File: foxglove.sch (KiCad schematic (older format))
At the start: 96 parts, among them IC1 LFE5U-12F-6BG256C, J1 NEIGHBOR1, J2 NEIGHBOR2, J3 Conn_02x05_Odd_Even, J4 Conn_02x10_Odd_Even, J5 Conn_01x02_Female, J6 Conn_02x03_Odd_Even, J7 BONUS_ROW, U1 LM393, U2 ADP225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

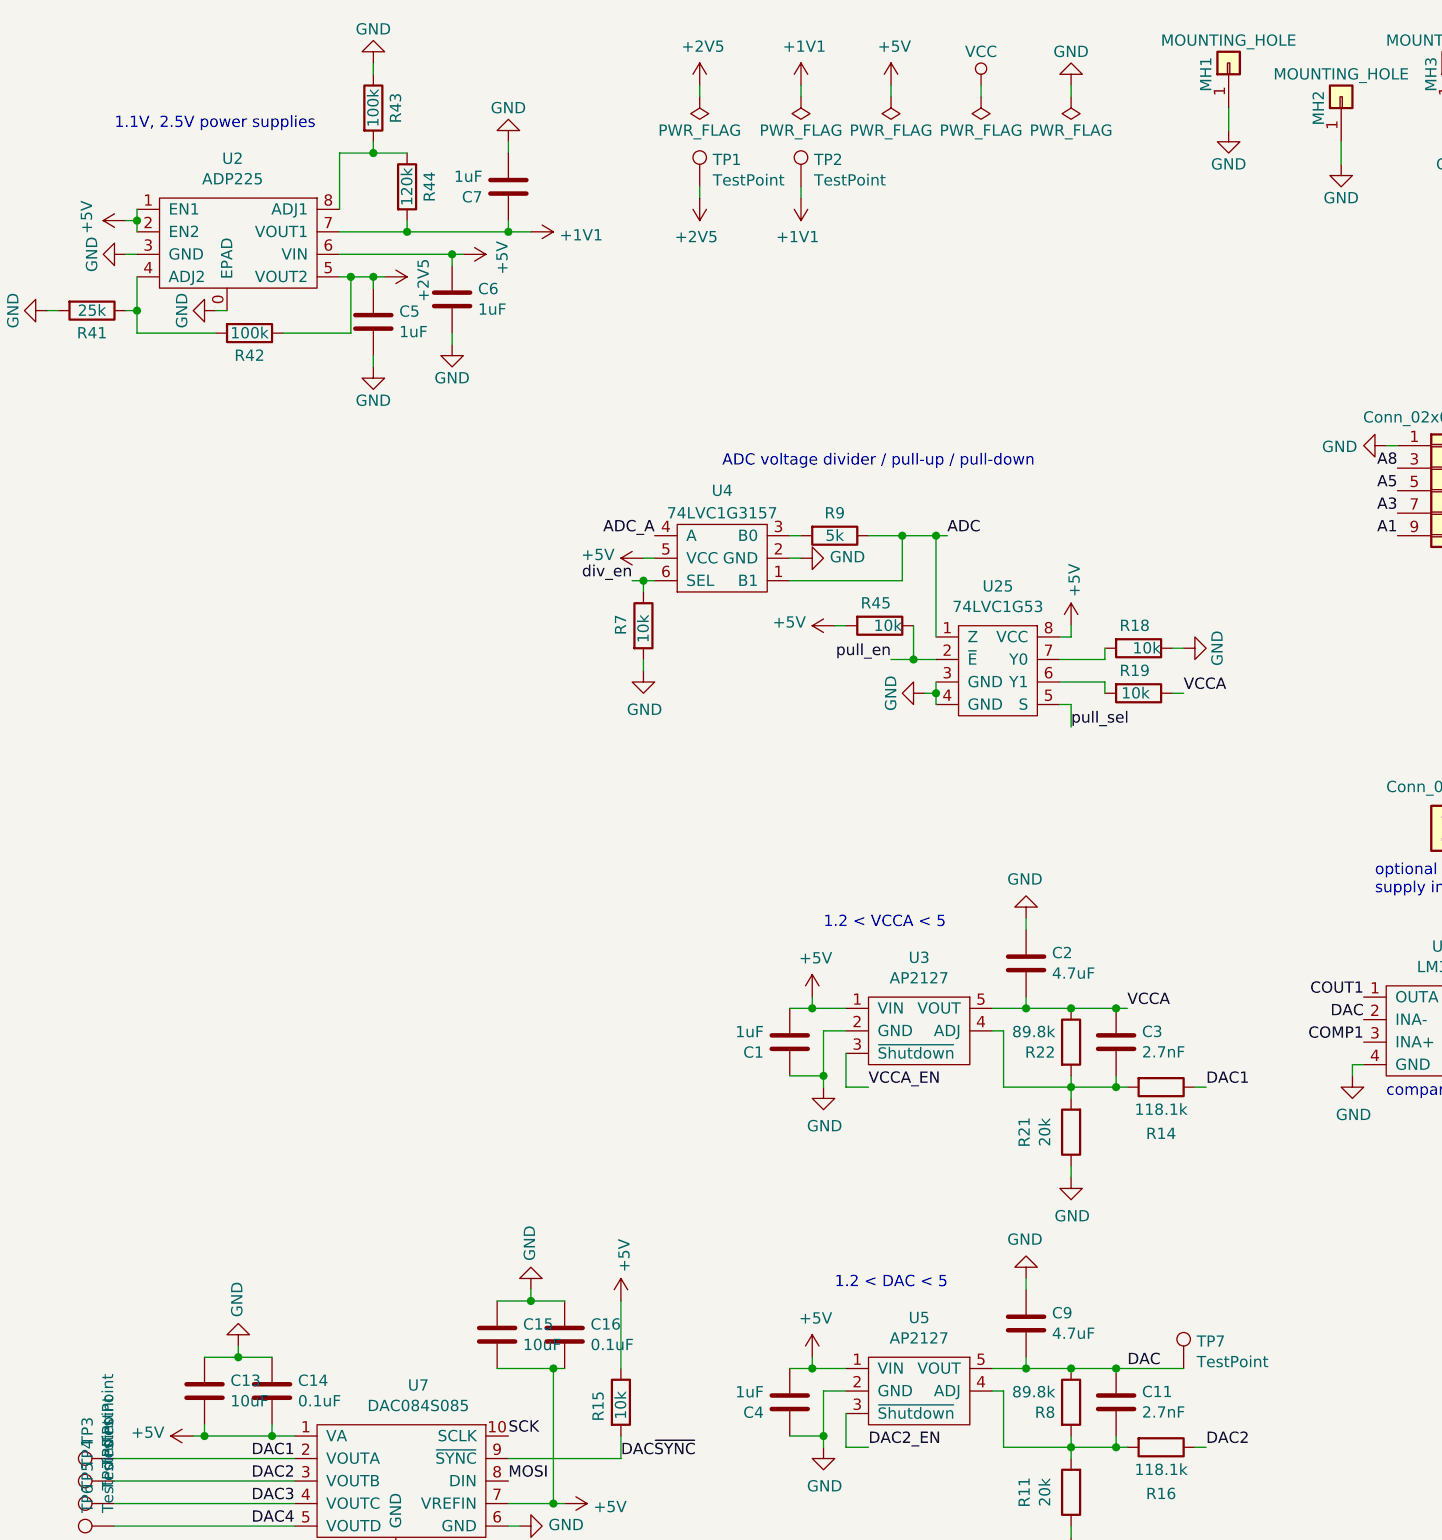
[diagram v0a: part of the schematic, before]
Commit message: Improved silkscreen table visibility and changed board edge cuts to support right-angle connectors
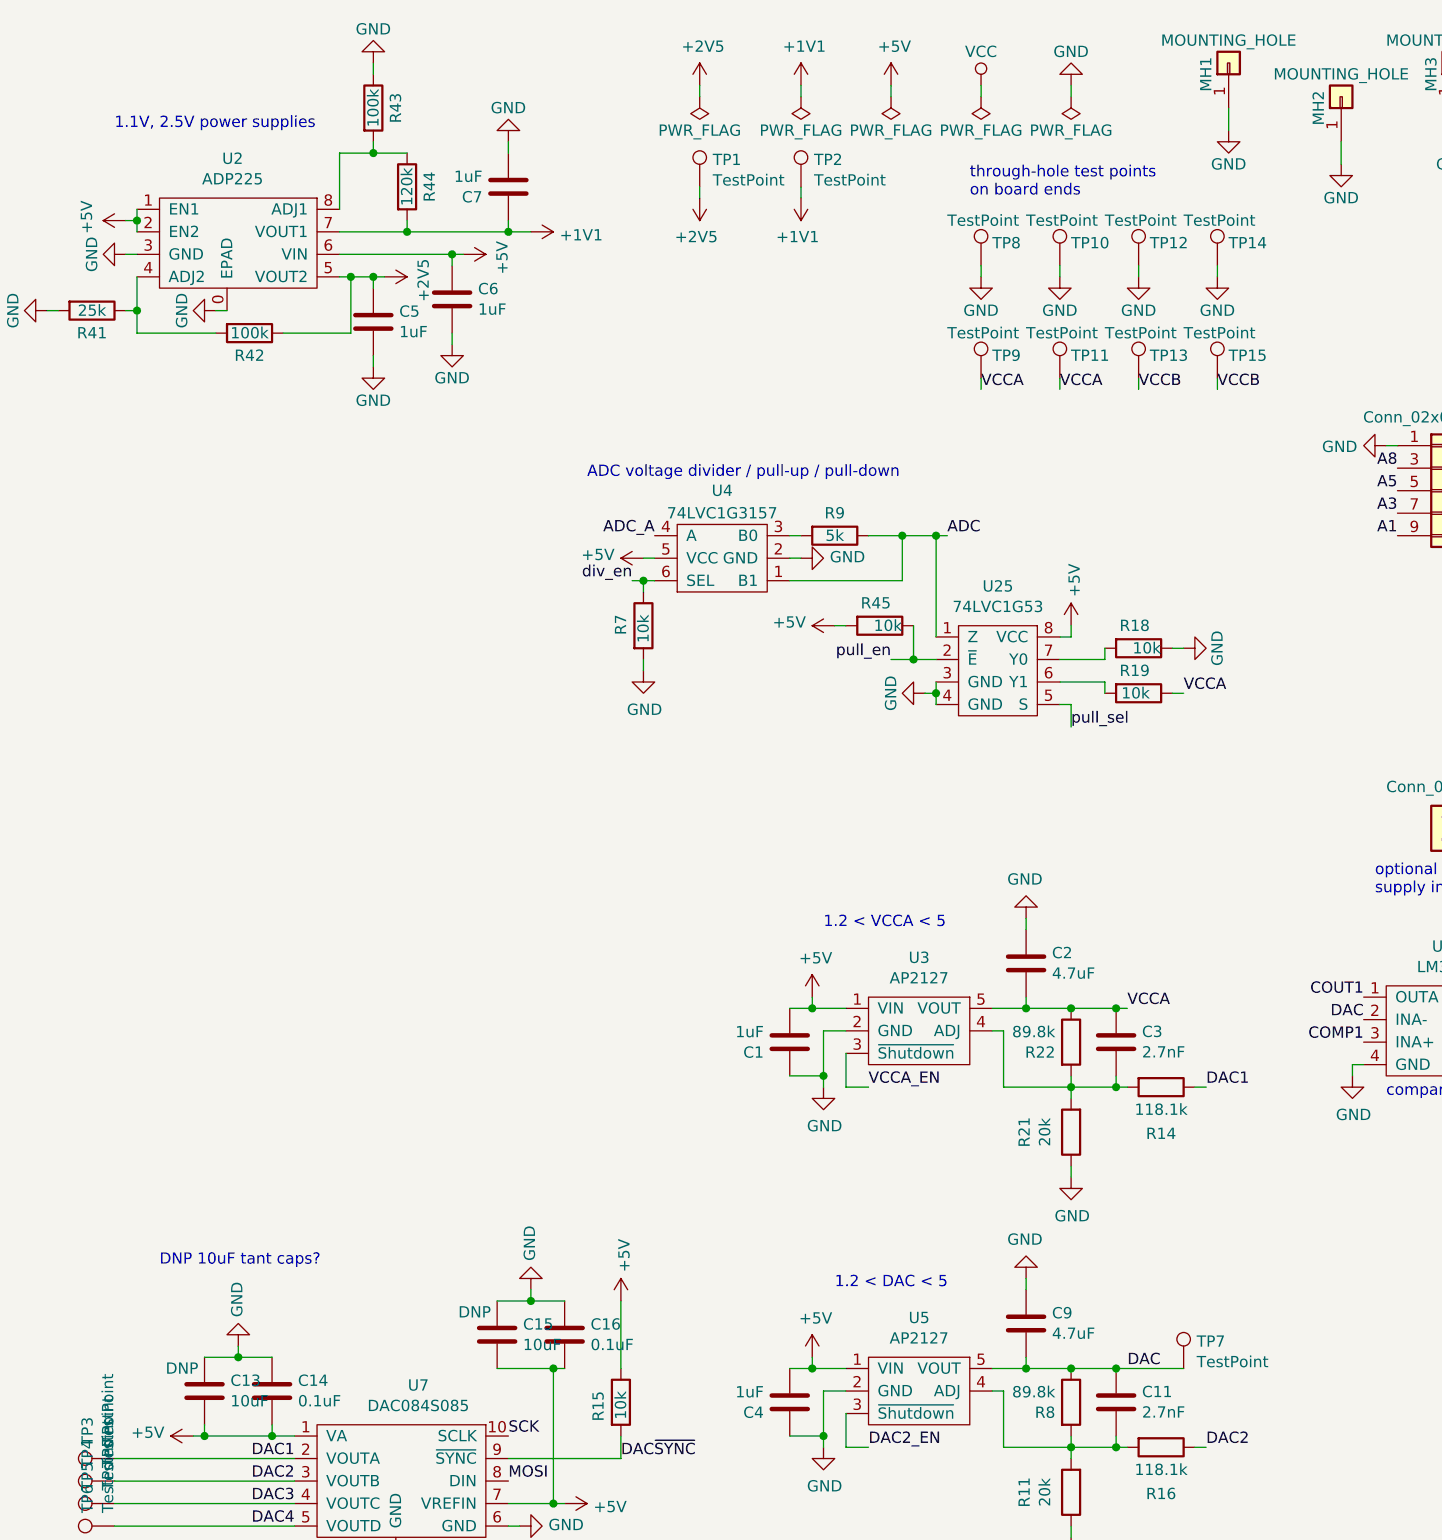
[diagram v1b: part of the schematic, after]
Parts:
- added TP10, TP12, TP14, TP8: TestPoint, gsg-modules:HEADER-1x1, symbol Connector:TestPoint
- added TP11, TP13, TP15, TP9: TestPoint, gsg-modules:HEADER-1x1-TESTPROBE, symbol Connector:TestPoint
- C13, C15: Note (none) -> DNP
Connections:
- net GND: now also TP10.1, TP12.1, TP14.1, TP8.1
- net VCCA: now also TP11.1, TP9.1
- net VCCB: now also TP13.1, TP15.1
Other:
- note added: "DNP 10uF tant caps?"
- note added: "through-hole test points\non board ends"
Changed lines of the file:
@@
 F 5 "F981A106MMA" H 10050 6700 50  0001 C CNN "Part Number"
 F 6 "CAP TANT 10UF 20% 10V 0603  " H 10050 6700 50  0001 C CNN "Description"
+F 7 "DNP" H 10150 6600 50  0000 C CNN "Note"
 	1    10050 6700
 	-1   0    0    1
@@
 Text Notes 12700 7800 0    50   ~ 0
 1.14 <VCCB < 3.465
-Text Notes 12350 2600 0    50   ~ 0
+Text Notes 11750 2650 0    50   ~ 0
 ADC voltage divider / pull-up / pull-down
 Text Notes 9650 1100 0    50   ~ 0
@@
 F 5 "F981A106MMA" H 11350 6450 50  0001 C CNN "Part Number"
 F 6 "CAP TANT 10UF 20% 10V 0603  " H 11350 6450 50  0001 C CNN "Description"
+F 7 "DNP" H 11450 6350 50  0000 C CNN "Note"
 	1    11350 6450
 	-1   0    0    1
@@
 	0    1    1    0
 $EndComp
-Wire Bus Line
-	-5400 2700 -3400 2700
-Wire Bus Line
-	-5700 3800 -3400 3800
-Wire Bus Line
-	-13800 8000 -10900 8000
-Wire Bus Line
-	-12700 9100 -10900 9100
-Wire Bus Line
-	-2150 4150 -400 4150
 $Comp
 L Device:R R?
@@
 	0    1    1    0
 $EndComp
+$Comp
+L Connector:TestPoint TP8
+U 1 1 5D434205
+P 13500 1700
+F 0 "TP8" H 13550 1800 50  0000 L CNN
+F 1 "TestPoint" H 13350 1900 50  0000 L CNN
+F 2 "gsg-modules:HEADER-1x1" H 13700 1700 50  0001 C CNN
+F 3 "~" H 13700 1700 50  0001 C CNN
+	1    13500 1700
+	1    0    0    -1
+$EndComp
+$Comp
+L power:GND #PWR0140
+U 1 1 5D4347AB
+P 13500 1750
+F 0 "#PWR0140" H 13500 1500 50  0001 C CNN
+F 1 "GND" H 13500 1600 50  0000 C CNN
+F 2 "" H 13500 1750 50  0001 C CNN
+F 3 "" H 13500 1750 50  0001 C CNN
+	1    13500 1750
+	1    0    0    -1
+$EndComp
+Wire Wire Line
+	13500 1700 13500 1750
+$Comp
+L Connector:TestPoint TP10
+U 1 1 5D4A93E9
+P 13850 1700
+F 0 "TP10" H 13900 1800 50  0000 L CNN
+F 1 "TestPoint" H 13700 1900 50  0000 L CNN
+F 2 "gsg-modules:HEADER-1x1" H 14050 1700 50  0001 C CNN
+F 3 "~" H 14050 1700 50  0001 C CNN
+	1    13850 1700
+	1    0    0    -1
+$EndComp
+$Comp
+L power:GND #PWR0141
+U 1 1 5D4A93F0
+P 13850 1750
+F 0 "#PWR0141" H 13850 1500 50  0001 C CNN
+F 1 "GND" H 13850 1600 50  0000 C CNN
+F 2 "" H 13850 1750 50  0001 C CNN
+F 3 "" H 13850 1750 50  0001 C CNN
+	1    13850 1750
+	1    0    0    -1
+$EndComp
+Wire Wire Line
+	13850 1700 13850 1750
+$Comp
+L Connector:TestPoint TP12
+U 1 1 5D4E3991
+P 14200 1700
+F 0 "TP12" H 14250 1800 50  0000 L CNN
+F 1 "TestPoint" H 14050 1900 50  0000 L CNN
+F 2 "gsg-modules:HEADER-1x1" H 14400 1700 50  0001 C CNN
+F 3 "~" H 14400 1700 50  0001 C CNN
+	1    14200 1700
+	1    0    0    -1
+$EndComp
+$Comp
+L power:GND #PWR0142
+U 1 1 5D4E3998
+P 14200 1750
+F 0 "#PWR0142" H 14200 1500 50  0001 C CNN
+F 1 "GND" H 14200 1600 50  0000 C CNN
+F 2 "" H 14200 1750 50  0001 C CNN
+F 3 "" H 14200 1750 50  0001 C CNN
+	1    14200 1750
+	1    0    0    -1
+$EndComp
+Wire Wire Line
+	14200 1700 14200 1750
+$Comp
+L Connector:TestPoint TP14
+U 1 1 5D4E399F
+P 14550 1700
+F 0 "TP14" H 14600 1800 50  0000 L CNN
+F 1 "TestPoint" H 14400 1900 50  0000 L CNN
+F 2 "gsg-modules:HEADER-1x1" H 14750 1700 50  0001 C CNN
+F 3 "~" H 14750 1700 50  0001 C CNN
+	1    14550 1700
+	1    0    0    -1
+$EndComp
+$Comp
+L power:GND #PWR0143
+U 1 1 5D4E39A6
+P 14550 1750
+F 0 "#PWR0143" H 14550 1500 50  0001 C CNN
+F 1 "GND" H 14550 1600 50  0000 C CNN
+F 2 "" H 14550 1750 50  0001 C CNN
+F 3 "" H 14550 1750 50  0001 C CNN
+	1    14550 1750
+	1    0    0    -1
+$EndComp
+Wire Wire Line
+	14550 1700 14550 1750
+$Comp
+L Connector:TestPoint TP9
+U 1 1 5D55A260
+P 13500 2200
+F 0 "TP9" H 13550 2300 50  0000 L CNN
+F 1 "TestPoint" H 13350 2400 50  0000 L CNN
+F 2 "gsg-modules:HEADER-1x1-TESTPROBE" H 13700 2200 50  0001 C CNN
+F 3 "~" H 13700 2200 50  0001 C CNN
+	1    13500 2200
+	1    0    0    -1
+$EndComp
+Wire Wire Line
+	13500 2200 13500 2250
+$Comp
+L Connector:TestPoint TP11
+U 1 1 5D55A26E
+P 13850 2200
+F 0 "TP11" H 13900 2300 50  0000 L CNN
+F 1 "TestPoint" H 13700 2400 50  0000 L CNN
+F 2 "gsg-modules:HEADER-1x1-TESTPROBE" H 14050 2200 50  0001 C CNN
+F 3 "~" H 14050 2200 50  0001 C CNN
+	1    13850 2200
+	1    0    0    -1
+$EndComp
+Wire Wire Line
+	13850 2200 13850 2250
+$Comp
+L Connector:TestPoint TP13
+U 1 1 5D55A27C
+P 14200 2200
+F 0 "TP13" H 14250 2300 50  0000 L CNN
+F 1 "TestPoint" H 14050 2400 50  0000 L CNN
+F 2 "gsg-modules:HEADER-1x1-TESTPROBE" H 14400 2200 50  0001 C CNN
+F 3 "~" H 14400 2200 50  0001 C CNN
+	1    14200 2200
+	1    0    0    -1
+$EndComp
+Wire Wire Line
+	14200 2200 14200 2250
+$Comp
+L Connector:TestPoint TP15
+U 1 1 5D55A28A
+P 14550 2200
+F 0 "TP15" H 14600 2300 50  0000 L CNN
+F 1 "TestPoint" H 14400 2400 50  0000 L CNN
+F 2 "gsg-modules:HEADER-1x1-TESTPROBE" H 14750 2200 50  0001 C CNN
+F 3 "~" H 14750 2200 50  0001 C CNN
+	1    14550 2200
+	1    0    0    -1
+$EndComp
+Wire Wire Line
+	14550 2200 14550 2250
+Wire Bus Line
+	-5400 2700 -3400 2700
+Wire Bus Line
+	-5700 3800 -3400 3800
+Wire Bus Line
+	-13800 8000 -10900 8000
+Wire Bus Line
+	-12700 9100 -10900 9100
+Wire Bus Line
+	-2150 4150 -400 4150
+Text Label 13500 2250 0    50   ~ 0
+VCCA
+Text Label 13850 2250 0    50   ~ 0
+VCCA
+Text Label 14200 2250 0    50   ~ 0
+VCCB
+Text Label 14550 2250 0    50   ~ 0
+VCCB
+Text Notes 13450 1400 0    50   ~ 0
+through-hole test points\non board ends
+Text Notes 9850 6150 0    50   ~ 0
+DNP 10uF tant caps?
 $EndSCHEMATC

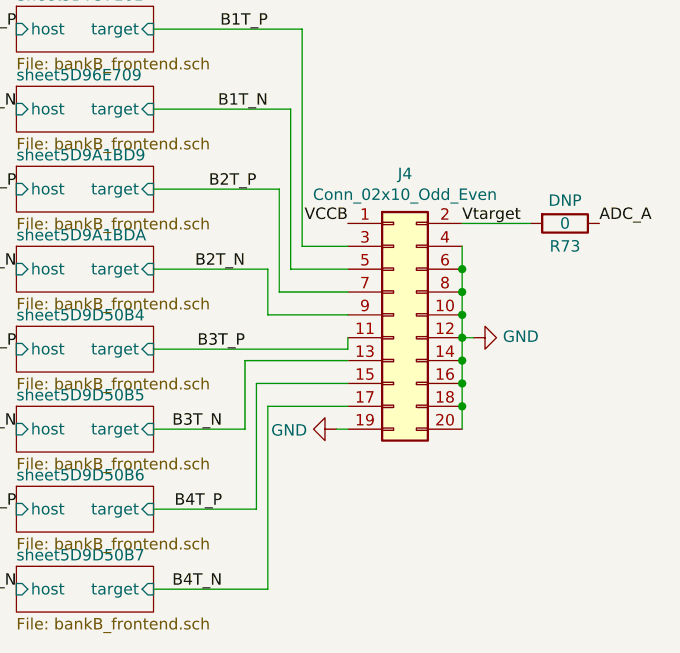
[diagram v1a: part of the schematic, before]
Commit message: Flipped J4 footprint
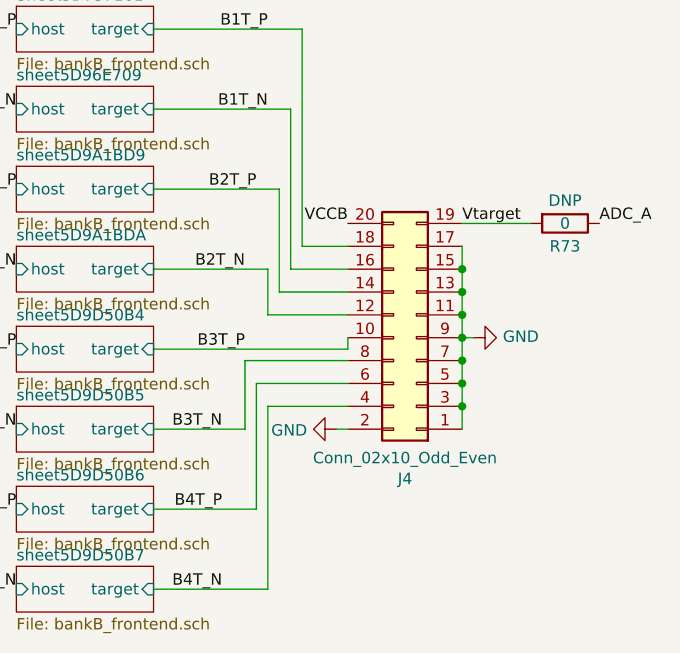
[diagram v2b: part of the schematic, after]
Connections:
- net B1T_N: now also J4.16 (Pin_16); no longer J4.5 (Pin_5)
- net B1T_P: now also J4.18 (Pin_18); no longer J4.3 (Pin_3)
- net B2T_N: now also J4.12 (Pin_12); no longer J4.9 (Pin_9)
- net B2T_P: now also J4.14 (Pin_14); no longer J4.7 (Pin_7)
- net B3T_N: now also J4.8 (Pin_8); no longer J4.13 (Pin_13)
- net B3T_P: now also J4.10 (Pin_10); no longer J4.11 (Pin_11)
- net B4T_N: now also J4.4 (Pin_4); no longer J4.17 (Pin_17)
- net B4T_P: now also J4.6 (Pin_6); no longer J4.15 (Pin_15)
- net GND: now also J4.1 (Pin_1), J4.11 (Pin_11), J4.13 (Pin_13), J4.15 (Pin_15), J4.17 (Pin_17), J4.2 (Pin_2), J4.3 (Pin_3), J4.5 (Pin_5), J4.7 (Pin_7), J4.9 (Pin_9); no longer J4.10 (Pin_10), J4.12 (Pin_12), J4.14 (Pin_14), J4.16 (Pin_16), J4.18 (Pin_18), J4.19 (Pin_19), J4.20 (Pin_20), J4.4 (Pin_4), J4.6 (Pin_6), J4.8 (Pin_8)
- net VCCB: now also J4.20 (Pin_20); no longer J4.1 (Pin_1)
- net Vtarget: now also J4.19 (Pin_19); no longer J4.2 (Pin_2)
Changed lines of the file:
@@
 L Connector_Generic:Conn_02x10_Odd_Even J4
 U 1 1 5D4FD960
-P 19350 1450
-F 0 "J4" H 19400 2067 50  0000 C CNN
-F 1 "Conn_02x10_Odd_Even" H 19400 1976 50  0000 C CNN
-F 2 "Connector_PinHeader_2.54mm:PinHeader_2x10_P2.54mm_Vertical" H 19350 1450 50  0001 C CNN
-F 3 "~" H 19350 1450 50  0001 C CNN
-F 4 "Sullins Connector Solutions" H 19350 1450 50  0001 C CNN "Manufacturer"
-F 5 "SBH11-PBPC-D10-RA-BK" H 19350 1450 50  0001 C CNN "Part Number"
-F 6 "CONN HEADER R/A 20POS 2.54MM" H 19350 1450 50  0001 C CNN "Description"
-	1    19350 1450
-	1    0    0    -1
+P 19450 1550
+F 0 "J4" H 19500 2167 50  0000 C CNN
+F 1 "Conn_02x10_Odd_Even" H 19500 2076 50  0000 C CNN
+F 2 "Connector_PinHeader_2.54mm:PinHeader_2x10_P2.54mm_Vertical" H 19450 1550 50  0001 C CNN
+F 3 "~" H 19450 1550 50  0001 C CNN
+F 4 "Sullins Connector Solutions" H 19450 1550 50  0001 C CNN "Manufacturer"
+F 5 "SBH11-PBPC-D10-RA-BK" H 19450 1550 50  0001 C CNN "Part Number"
+F 6 "CONN HEADER R/A 20POS 2.54MM" H 19450 1550 50  0001 C CNN "Description"
+	1    19450 1550
+	-1   0    0    1
 $EndComp
 Text Label 19150 1050 2    50   ~ 0
@@
 Wire Wire Line
 	14550 2200 14550 2250
-Wire Bus Line
-	-5400 2700 -3400 2700
-Wire Bus Line
-	-5700 3800 -3400 3800
-Wire Bus Line
-	-13800 8000 -10900 8000
-Wire Bus Line
-	-12700 9100 -10900 9100
-Wire Bus Line
-	-2150 4150 -400 4150
 Text Label 13500 2250 0    50   ~ 0
 VCCA
@@
 Text Notes 9850 6150 0    50   ~ 0
 DNP 10uF tant caps?
+Wire Bus Line
+	-5400 2700 -3400 2700
+Wire Bus Line
+	-5700 3800 -3400 3800
+Wire Bus Line
+	-13800 8000 -10900 8000
+Wire Bus Line
+	-12700 9100 -10900 9100
+Wire Bus Line
+	-2150 4150 -400 4150
 $EndSCHEMATC

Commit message: schematic: cleanup and squish onto a page
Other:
- note added: "Analog Frontend"
- note added: "Bank A"
- note added: "Bank B"
- note added: "Digital Frontend"
- note added: "FPGA"
- note added: "FPGA Supplies"
- note added: "I/O Supplies"
- note added: "Input & Output"
- note added: "Supply Conditioning (Decoupling)"
- note added: "Test Points & Power Distribution"
- note added: "board end TPs"
- note added: "optional: SPI flash for configuration"
- note added: "— KT: supply TDP too high for package;\nreplace w/ better heatsinked package or\ninline thermal resistor"
- note removed: "check digital levels\nfor mux (5V)"
- note removed: "optional SPI flash"
- note removed: "through-hole test points\non board ends"
- moved on the sheet: C1, C10, C11, C12, C13, C14, C15, C16, C18, C19, C2, C21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

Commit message: adopt OSHWA convention for SPI signal names https://www.oshwa.org/a-resolution-to-redefine-spi-signal-names
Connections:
- net MISO renamed CIPO
- net MOSI renamed COPI
- net SSEL renamed CS
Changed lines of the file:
@@
 	14100 1050 14100 1000
 Text Label 15900 3650 3    50   ~ 0
-SSEL
+CS
 Text Label 15900 3150 1    50   ~ 0
 SCK
 Text Label 16000 3650 3    50   ~ 0
-MOSI
+COPI
 Text Label 16000 3150 1    50   ~ 0
-MISO
+CIPO
 Wire Wire Line
 	14100 1600 14100 1550
@@
 SCK
 Text Label 8350 1700 0    50   ~ 0
-MOSI
+COPI
 Text Label 8850 1600 0    50   ~ 0
 DAC~SYNC~
@@
 J1.26
 Text Label 3300 8500 3    50   ~ 0
-SSEL
+CS
 Text Label 3500 8500 3    50   ~ 0
 J1.23
@@
 	6150 9450 6150 8950
 Text Label 1700 8500 3    50   ~ 0
-MOSI
+COPI
 Text Label 1800 8500 3    50   ~ 0
-MISO
+CIPO
 Text Label 2300 8500 3    50   ~ 0
 J1.16
@@
 CSSPIN
 Text Label 11500 9800 0    50   ~ 0
-MOSI
+COPI
 Text Label 11500 9900 0    50   ~ 0
-MISO
+CIPO
 $Comp
 L power:VCC #PWR0120
